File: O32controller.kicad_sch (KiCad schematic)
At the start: 18 parts, among them J1 Conn_01x08_MountingPin, J2 BATT+, J3 BATT-, U2 STSPIN32F0A

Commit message: before big shunt:
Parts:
- added C11: 1nF, Capacitor_SMD:C_0402_1005Metric, symbol Device:C_Small
- added R14, R17, R20: 2.2k, Resistor_SMD:R_0402_1005Metric, symbol Device:R_Small_US
- added R22: 121k, Resistor_SMD:R_0402_1005Metric, symbol Device:R_Small_US
- C10: value 10nF -> 100nF
- D1: value STPS1L60A -> SBA0540Q; footprint (none) -> Diode_SMD:D_DFN2L
- D2: value D_TVS -> ESDA17P20-1F2; footprint (none) -> Diode_SMD:D_0402_CSP
- gave numbers to parts that had none: 1
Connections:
- net GPIO_PF0 is gone; now on net OP_V_O: U2.4 (PF0)
- net GPIO_PF1 is gone; now on net OP_W_O: U2.5 (PF1)
- net +3.3V: now also U1.11 (VDD), R22.1
- net GND: now also J1.8 (Pin_8), C11.2; no longer J1.4 (Pin_4)
- net OC_COMP: now also C11.1, R14.1, R17.1, R20.1, R22.2
- net OP_U_O: now also U2.19 (PB1)
- net GPIO_PA15: now reaches U2.39 (PA15)
- net GPIO_PA15: now also J1.4 (Pin_4)
- new net Motor phase U/SENSE_P: R14.2
- new net Motor phase V/SENSE_P: R17.2
- new net Motor phase W/SENSE_P: R20.2
- no-connect marks 9 -> 8
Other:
- sheet Motor phase U ports: added SENSE_P; removed none
- sheet Motor phase V ports: added SENSE_P; removed none
- sheet Motor phase W ports: added SENSE_P; removed none
- note added: "Probably break out a through hole for each"
- note added: "TVS clamp to 23V"
- note added: "with the 100mA comparator setting 121k limits transient current to 60A. https://www.desmos.com/calculator/u6fciyrjnf"
- note removed: "TVS clamp to 15V"
- moved on the sheet: C1, C2, C3, C4, C5, C6, C7, C8, C9, D1, D2, J1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

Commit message: routed some more
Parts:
- added J7: BATT+, O32controller:SolderWire-Actual_1x01_D1.7mm_OD_2.75mm, symbol Connector_Generic:Conn_01x01
- added J8: BATT-, O32controller:SolderWire-Actual_1x01_D1.7mm_OD_2.75mm, symbol Connector_Generic:Conn_01x01
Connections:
- net GND: now also J8.1 (Pin_1)
- net VBUS: now also J7.1 (Pin_1)
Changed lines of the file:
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@@
     (date "2022-11-26")
   )
+  (junction (at 255.27 22.86) (diameter 0) (color 0 0 0 0)
+  )
   (junction (at 163.83 41.91) (diameter 0) (color 0 0 0 0)
   )
@@
   )
   (junction (at 232.41 35.56) (diameter 0) (color 0 0 0 0)
+  )
+  (junction (at 255.27 40.64) (diameter 0) (color 0 0 0 0)
   )
   (junction (at 255.27 27.94) (diameter 0) (color 0 0 0 0)
@@
     (stroke (width 0) (type default) (color 0 0 0 0))
   )
-  (wire (pts (xy 255.27 26.67) (xy 255.27 27.94))
+  (wire (pts (xy 255.27 20.32) (xy 255.27 22.86))
     (stroke (width 0) (type default) (color 0 0 0 0))
   )
@@
     (stroke (width 0) (type default) (color 0 0 0 0))
   )
+  (wire (pts (xy 255.27 22.86) (xy 255.27 27.94))
+    (stroke (width 0) (type default) (color 0 0 0 0))
+  )
   (wire (pts (xy 24.13 87.63) (xy 31.75 87.63))
     (stroke (width 0) (type default) (color 0 0 0 0))
@@
     (stroke (width 0) (type default) (color 0 0 0 0))
   )
-  (wire (pts (xy 255.27 35.56) (xy 255.27 36.83))
+  (wire (pts (xy 255.27 35.56) (xy 255.27 40.64))
     (stroke (width 0) (type default) (color 0 0 0 0))
   )
@@
   )
   (wire (pts (xy 204.47 130.81) (xy 196.85 130.81))
+    (stroke (width 0) (type default) (color 0 0 0 0))
+  )
+  (wire (pts (xy 255.27 40.64) (xy 255.27 43.18))
     (stroke (width 0) (type default) (color 0 0 0 0))
   )
@@
       (effects (font (size 1.27 1.27)) hide)
     )
-    (property "Datasheet" "~" (id 3) (at 129.54 39.37 90)
+    (property "Datasheet" "https://www.digikey.com/en/products/detail/panjit-international-inc/SBA0540Q-R1-00001/14661073" (id 3) (at 129.54 39.37 90)
       (effects (font (size 1.27 1.27)) hide)
     )
@@
     (pin "1")
   )
+  (symbol (lib_id "Connector_Generic:Conn_01x01") (at 260.35 40.64 0) (unit 1)
+    (in_bom yes) (on_board yes) (fields_autoplaced)
+    (property "Reference" "J8" (id 0) (at 262.89 39.3699 0)
+      (effects (font (size 1.27 1.27)) (justify left))
+    )
+    (property "Value" "BATT-" (id 1) (at 262.89 41.9099 0)
+      (effects (font (size 1.27 1.27)) (justify left))
+    )
+    (property "Footprint" "O32controller:SolderWire-Actual_1x01_D1.7mm_OD_2.75mm" (id 2) (at 260.35 40.64 0)
+      (effects (font (size 1.27 1.27)) hide)
+    )
+    (property "Datasheet" "~" (id 3) (at 260.35 40.64 0)
+      (effects (font (size 1.27 1.27)) hide)
+    )
+    (pin "1")
+  )
   (symbol (lib_id "power:GND") (at 163.83 50.8 0) (unit 1)
     (in_bom yes) (on_board yes)
@@
     (pin "9")
   )
-  (symbol (lib_id "power:VBUS") (at 255.27 26.67 0) (unit 1)
-    (in_bom yes) (on_board yes) (fields_autoplaced)
-    (property "Reference" "#PWR010" (id 0) (at 255.27 30.48 0)
-      (effects (font (size 1.27 1.27)) hide)
-    )
-    (property "Value" "VBUS" (id 1) (at 255.27 21.59 0))
-    (property "Footprint" "" (id 2) (at 255.27 26.67 0)
-      (effects (font (size 1.27 1.27)) hide)
-    )
-    (property "Datasheet" "" (id 3) (at 255.27 26.67 0)
+  (symbol (lib_id "power:VBUS") (at 255.27 20.32 0) (unit 1)
+    (in_bom yes) (on_board yes) (fields_autoplaced)
+    (property "Reference" "#PWR010" (id 0) (at 255.27 24.13 0)
+      (effects (font (size 1.27 1.27)) hide)
+    )
+    (property "Value" "VBUS" (id 1) (at 255.27 15.24 0))
+    (property "Footprint" "" (id 2) (at 255.27 20.32 0)
+      (effects (font (size 1.27 1.27)) hide)
+    )
+    (property "Datasheet" "" (id 3) (at 255.27 20.32 0)
       (effects (font (size 1.27 1.27)) hide)
     )
@@
     (pin "2")
   )
+  (symbol (lib_id "Connector_Generic:Conn_01x01") (at 260.35 22.86 0) (unit 1)
+    (in_bom yes) (on_board yes) (fields_autoplaced)
+    (property "Reference" "J7" (id 0) (at 262.89 21.5899 0)
+      (effects (font (size 1.27 1.27)) (justify left))
+    )
+    (property "Value" "BATT+" (id 1) (at 262.89 24.1299 0)
+      (effects (font (size 1.27 1.27)) (justify left))
+    )
+    (property "Footprint" "O32controller:SolderWire-Actual_1x01_D1.7mm_OD_2.75mm" (id 2) (at 260.35 22.86 0)
+      (effects (font (size 1.27 1.27)) hide)
+    )
+    (property "Datasheet" "~" (id 3) (at 260.35 22.86 0)
+      (effects (font (size 1.27 1.27)) hide)
+    )
+    (pin "1")
+  )
   (symbol (lib_id "power:GND") (at 116.84 44.45 0) (unit 1)
     (in_bom yes) (on_board yes) (fields_autoplaced)
@@
     (pin "1")
   )
-  (symbol (lib_id "power:GND") (at 255.27 36.83 0) (unit 1)
-    (in_bom yes) (on_board yes) (fields_autoplaced)
-    (property "Reference" "#PWR011" (id 0) (at 255.27 43.18 0)
-      (effects (font (size 1.27 1.27)) hide)
-    )
-    (property "Value" "GND" (id 1) (at 255.27 41.91 0))
-    (property "Footprint" "" (id 2) (at 255.27 36.83 0)
-      (effects (font (size 1.27 1.27)) hide)
-    )
-    (property "Datasheet" "" (id 3) (at 255.27 36.83 0)
+  (symbol (lib_id "power:GND") (at 255.27 43.18 0) (unit 1)
+    (in_bom yes) (on_board yes) (fields_autoplaced)
+    (property "Reference" "#PWR011" (id 0) (at 255.27 49.53 0)
+      (effects (font (size 1.27 1.27)) hide)
+    )
+    (property "Value" "GND" (id 1) (at 255.27 48.26 0))
+    (property "Footprint" "" (id 2) (at 255.27 43.18 0)
+      (effects (font (size 1.27 1.27)) hide)
+    )
+    (property "Datasheet" "" (id 3) (at 255.27 43.18 0)
       (effects (font (size 1.27 1.27)) hide)
     )
@@
       (reference "J6") (unit 1) (value "Motor Connection") (footprint "O32controller:SolderWire-Actual_1x01_D1.7mm_OD_2.75mm")
     )
+    (path "/db0c424b-9158-4edb-876a-613bcf0e8781"
+      (reference "J7") (unit 1) (value "BATT+") (footprint "O32controller:SolderWire-Actual_1x01_D1.7mm_OD_2.75mm")
+    )
+    (path "/5b47419e-dce2-4024-8b80-ee858fd83735"
+      (reference "J8") (unit 1) (value "BATT-") (footprint "O32controller:SolderWire-Actual_1x01_D1.7mm_OD_2.75mm")
+    )
     (path "/6c4baef6-fdf2-4afa-9619-12d184d04052"
       (reference "L1") (unit 1) (value "22uH") (footprint "O32controller:IND_VLS201612CX-220M-1")
@@
     )
     (path "/afcdcb47-145e-4051-91ad-5d7b960fbb25/1dc0362a-2019-452e-8829-c688c9b4e4a8"
-      (reference "R23") (unit 1) (value "2.21R") (footprint "Resistor_SMD:R_0402_1005Metric")
+      (reference "R23") (unit 1) (value "2.2R") (footprint "Resistor_SMD:R_0402_1005Metric")
     )
     (path "/801c7eb0-ff7a-4793-a702-7472e29bc37a/1dc0362a-2019-452e-8829-c688c9b4e4a8"
-      (reference "R24") (unit 1) (value "2.21R") (footprint "Resistor_SMD:R_0402_1005Metric")
+      (reference "R24") (unit 1) (value "2.2R") (footprint "Resistor_SMD:R_0402_1005Metric")
     )
     (path "/d1474dce-644b-4913-80b1-6962d0581a1a/1dc0362a-2019-452e-8829-c688c9b4e4a8"
-      (reference "R25") (unit 1) (value "2.21R") (footprint "Resistor_SMD:R_0402_1005Metric")
+      (reference "R25") (unit 1) (value "2.2R") (footprint "Resistor_SMD:R_0402_1005Metric")
     )
     (path "/78fefdae-d615-4cae-96c5-e100df976e99"

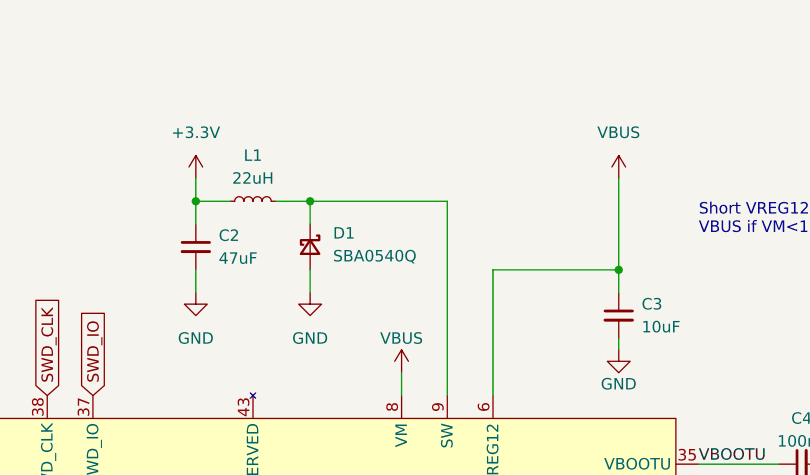
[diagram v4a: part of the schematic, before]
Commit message: routed most of power stage, no drc violations
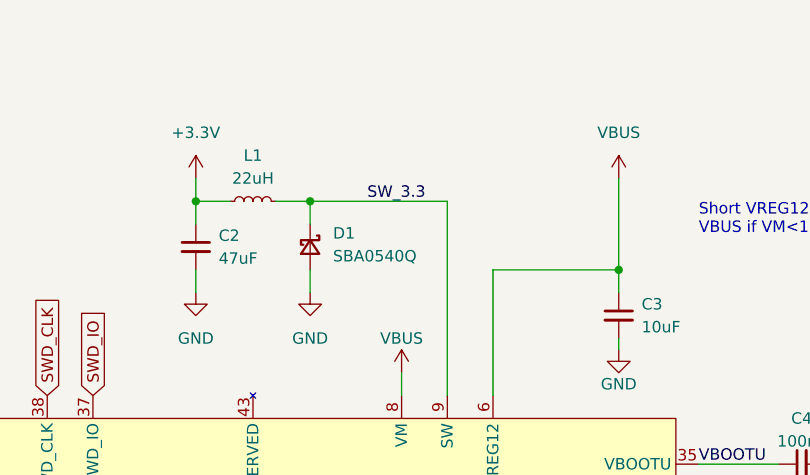
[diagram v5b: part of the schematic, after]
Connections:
- net SW_3.3: now reaches D1.1 (K), L1.2, U2.9 (SW)
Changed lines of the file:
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@@
+    (effects (font (size 1.27 1.27)) (justify left bottom))
+  )
+  (label "SW_3.3" (at 135.89 34.29 0)
     (effects (font (size 1.27 1.27)) (justify left bottom))
   )

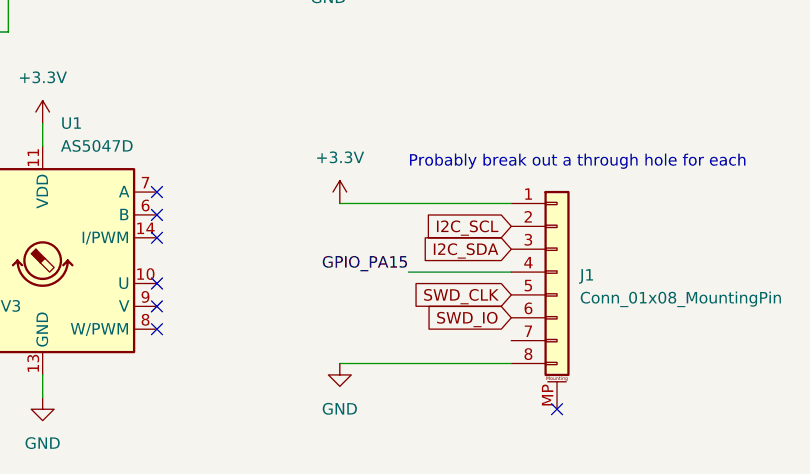
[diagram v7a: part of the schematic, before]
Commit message: just need to figure out gpio and buck
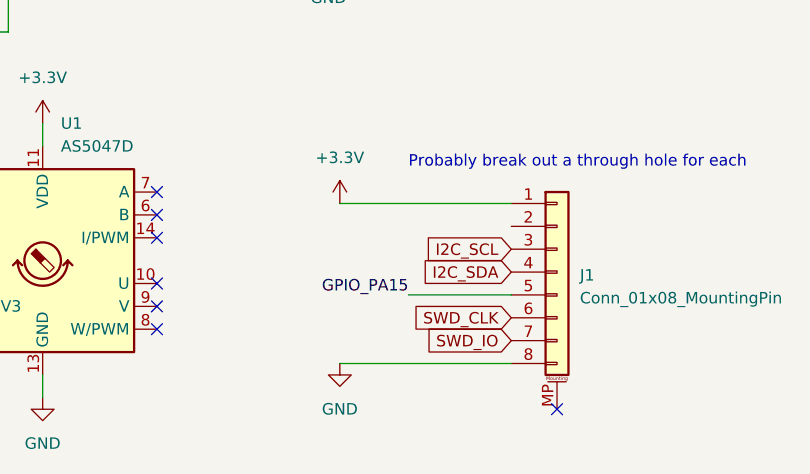
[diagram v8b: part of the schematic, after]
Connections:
- net GPIO_PA15: now also J1.5 (Pin_5); no longer J1.4 (Pin_4)
- net I2C_SCL: now also J1.3 (Pin_3); no longer J1.2 (Pin_2)
- net I2C_SDA: now also J1.4 (Pin_4); no longer J1.3 (Pin_3)
- net SWD_CLK: now also J1.6 (Pin_6); no longer J1.5 (Pin_5)
- net SWD_IO: now also J1.7 (Pin_7); no longer J1.6 (Pin_6)
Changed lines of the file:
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@@
     (stroke (width 0) (type default) (color 0 0 0 0))
   )
-  (wire (pts (xy 102.87 172.72) (xy 114.3 172.72))
+  (wire (pts (xy 102.87 175.26) (xy 114.3 175.26))
     (stroke (width 0) (type default) (color 0 0 0 0))
   )
@@
     (effects (font (size 1.27 1.27)) (justify left bottom))
   )
-  (label "GPIO_PA15" (at 102.87 172.72 180)
+  (label "GPIO_PA15" (at 102.87 175.26 180)
     (effects (font (size 1.27 1.27)) (justify right bottom))
   )
@@
     (effects (font (size 1.27 1.27)) (justify left bottom))
   )
-  (global_label "SWD_IO" (shape input) (at 114.3 177.8 180) (fields_autoplaced)
-    (effects (font (size 1.27 1.27)) (justify right))
-    (property "Intersheet References" "${INTERSHEET_REFS}" (id 0) (at 105.0531 177.8794 0)
-      (effects (font (size 1.27 1.27)) (justify right) hide)
-    )
-  )
-  (global_label "I2C_SDA" (shape input) (at 114.3 170.18 180) (fields_autoplaced)
-    (effects (font (size 1.27 1.27)) (justify right))
-    (property "Intersheet References" "${INTERSHEET_REFS}" (id 0) (at 104.2669 170.2594 0)
+  (global_label "SWD_IO" (shape input) (at 114.3 180.34 180) (fields_autoplaced)
+    (effects (font (size 1.27 1.27)) (justify right))
+    (property "Intersheet References" "${INTERSHEET_REFS}" (id 0) (at 105.0531 180.4194 0)
+      (effects (font (size 1.27 1.27)) (justify right) hide)
+    )
+  )
+  (global_label "I2C_SDA" (shape input) (at 114.3 172.72 180) (fields_autoplaced)
+    (effects (font (size 1.27 1.27)) (justify right))
+    (property "Intersheet References" "${INTERSHEET_REFS}" (id 0) (at 104.2669 172.7994 0)
       (effects (font (size 1.27 1.27)) (justify right) hide)
     )
@@
     )
   )
-  (global_label "SWD_CLK" (shape input) (at 114.3 175.26 180) (fields_autoplaced)
-    (effects (font (size 1.27 1.27)) (justify right))
-    (property "Intersheet References" "${INTERSHEET_REFS}" (id 0) (at 103.4202 175.3394 0)
+  (global_label "SWD_CLK" (shape input) (at 114.3 177.8 180) (fields_autoplaced)
+    (effects (font (size 1.27 1.27)) (justify right))
+    (property "Intersheet References" "${INTERSHEET_REFS}" (id 0) (at 103.4202 177.8794 0)
       (effects (font (size 1.27 1.27)) (justify right) hide)
     )
@@
     )
   )
-  (global_label "I2C_SCL" (shape input) (at 114.3 167.64 180) (fields_autoplaced)
-    (effects (font (size 1.27 1.27)) (justify right))
-    (property "Intersheet References" "${INTERSHEET_REFS}" (id 0) (at 104.3274 167.7194 0)
-      (effects (font (size 1.27 1.27)) (justify right) hide)
-    )
+  (global_label "I2C_SCL" (shape input) (at 114.3 170.18 180) (fields_autoplaced)
+    (effects (font (size 1.27 1.27)) (justify right))
+    (property "Intersheet References" "${INTERSHEET_REFS}" (id 0) (at 104.3274 170.2594 0)
+      (effects (font (size 1.27 1.27)) (justify right) hide)
+    )
